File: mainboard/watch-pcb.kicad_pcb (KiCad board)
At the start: 6 copper layers, 42 x 42 mm, 179 parts, among them J10 LASER-, J11 MTR+, J13 MTR-, J2 USB_C_Receptacle, J3 ESP_ANT, J5 Micro_SD_Card, J6 TT143AMC12C, J7 BATT+, J8 BATT-, J9 LASER+, Q1 BSS214NW, Q2 BSS138, Q3 BSS138, SW1 B3U-3000P-B, SW2 B3U-3000P-B, SW3 B3U-3000P-B, SW4 B3U-3000P-B, SW8 BOOT, U1 TPS63021, U10 LIS3MDL, U11 ESP32-S3, U12 LSM6DSOXTR, U13 DRV2605LDGS, U14 MAX30102, U15 APDS-9306-065, U16 AP3019AK, U17 TLV62569DDC, U2 BQ25628E, U3 BME280, U4 BQ27427YZFR, U5 MX25UM51245GXDI00, U6 S80KS5123GABHV020, U8 TCA9535MRGER, U9 TPS65631W, Y1 32.768kHz, Y2 40MHz(10ppm)

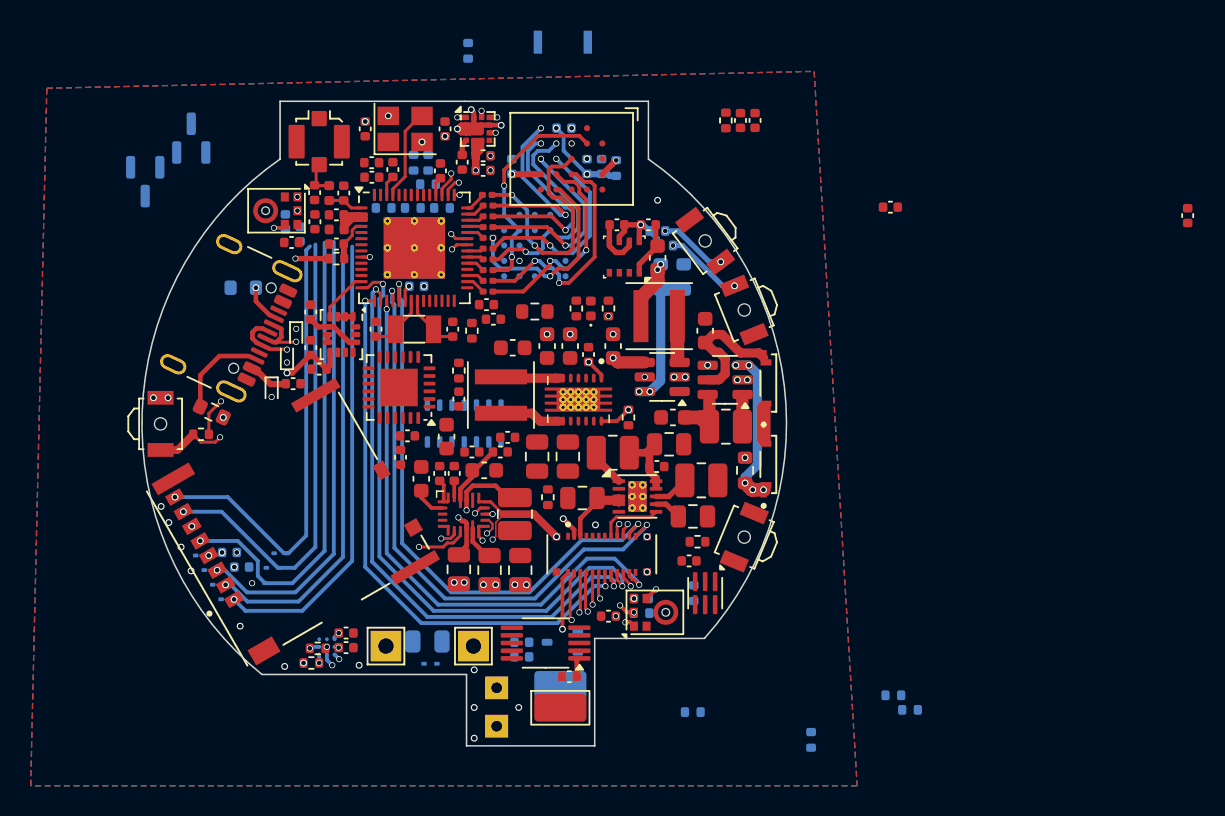
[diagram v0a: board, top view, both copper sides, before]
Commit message: mostly cleaned pcb after removals
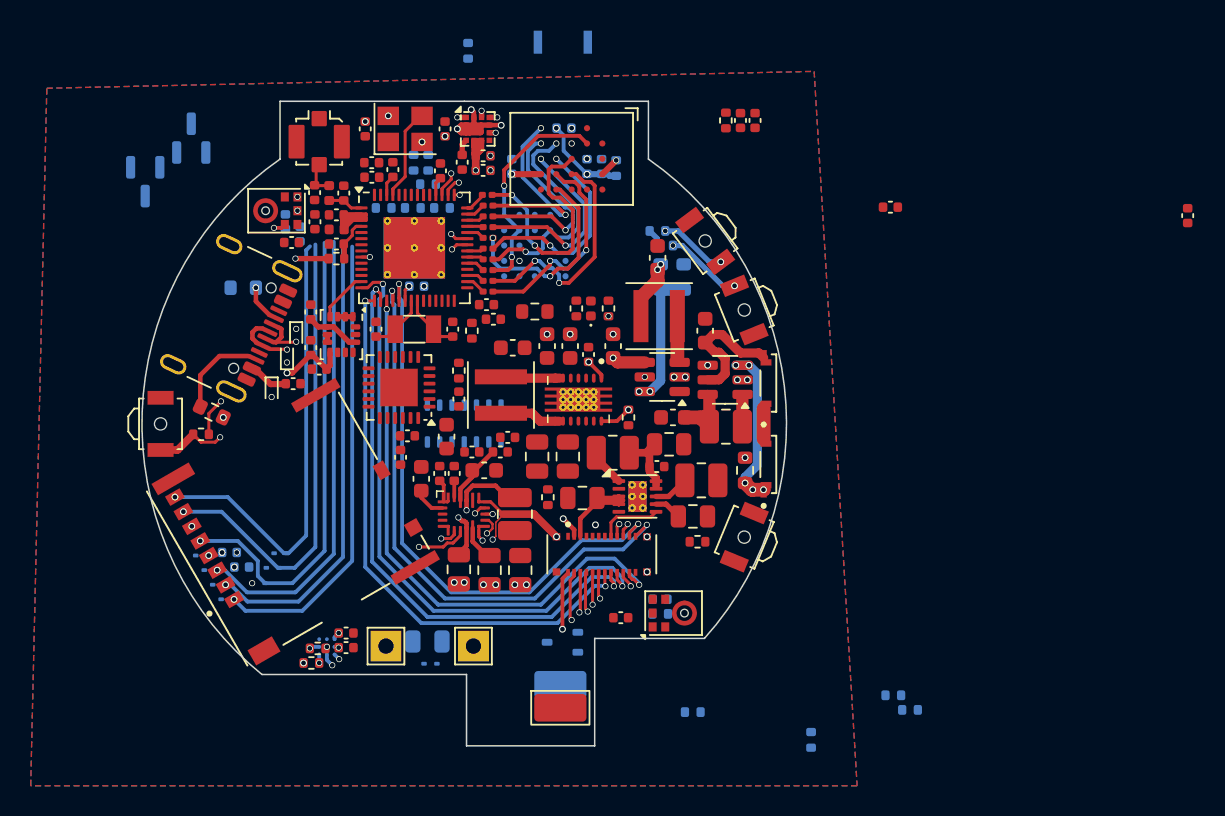
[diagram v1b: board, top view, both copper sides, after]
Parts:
- removed C52, C75, C78: 1uF, Capacitor_SMD:C_0402_1005Metric
- removed C54, C62, C71: 100nF, Capacitor_SMD:C_0402_1005Metric
- removed J11: MTR+, TestPoint:TestPoint_THTPad_1.5x1.5mm_Drill0.7mm
- removed J13: MTR-, TestPoint:TestPoint_THTPad_1.5x1.5mm_Drill0.7mm
- removed R5: 100k, Resistor_SMD:R_0402_1005Metric
- removed U13: DRV2605LDGS, Package_SO:VSSOP-10_3x3mm_P0.5mm
- removed U15: APDS-9306-065, OptoDevice:Broadcom_DFN-6_2x2mm_P0.65mm
- removed U3: BME280, Package_LGA:Bosch_LGA-8_2.5x2.5mm_P0.65mm_ClockwisePinNumbering
- moved R45 1.22 mm to (162.8, 95.9)
- moved C68 1.22 mm to (162.8, 95.0)
- moved MK2 1.22 mm to (163.6, 95.8)
- moved R36 0.81 mm to (160.2, 96.2)
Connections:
- J6 pad 15: /ESP MCU/EXT_IO3 -> /ESP MCU/EXT_IO2
- J6 pad 5: /ESP MCU/EXT_IO2 -> /ESP MCU/EXT_IO1
- R14 pad 1: /ESP MCU/EXT_IO10 -> /ESP MCU/EXT_IO9
- R15 pad 1: /ESP MCU/EXT_IO11 -> /ESP MCU/EXT_IO8
- R17 pad 1: /ESP MCU/EXT_IO12 -> /ESP MCU/EXT_IO7
- R47 pad 2: /ESP MCU/EXT_IO5 -> /ESP MCU/EXT_IO3
- R48 pad 2: /ESP MCU/EXT_IO6 -> /ESP MCU/EXT_IO4
- R49 pad 2: /ESP MCU/EXT_IO7 -> /ESP MCU/EXT_IO5
- SW2 pad 1: /ESP MCU/EXT_IO5 -> /ESP MCU/EXT_IO3
- SW3 pad 2: /ESP MCU/EXT_IO6 -> /ESP MCU/EXT_IO4
- SW4 pad 1: /ESP MCU/EXT_IO7 -> /ESP MCU/EXT_IO5
- U1 pad 13: /ESP MCU/EXT_IO10 -> /ESP MCU/EXT_IO9
- U10 pad 7: /ESP MCU/EXT_IO9 -> /ESP MCU/EXT_IO6
- U12 pad 9: /ESP MCU/EXT_IO4 -> /ESP MCU/IO7
- U2 pad 11: /ESP MCU/EXT_IO11 -> /ESP MCU/EXT_IO8
- U4 pad A1: /ESP MCU/EXT_IO12 -> /ESP MCU/EXT_IO7
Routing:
- net +3V3: track 48.0 -> 38.4 mm, vias 12 -> 10
- net GND: track 28.3 -> 21.4 mm, vias 54 -> 40
- net /ESP MCU/I2S_SCK: track 72.1 -> 65.4 mm, vias 3 -> 2
- net /ESP MCU/EXT_IO5: track 0.00 -> 5.10 mm, vias 0 -> 2
- net /ESP MCU/EXT_IO7: track 5.10 -> 0.55 mm, vias 2 -> 1
- net /ESP MCU/EXT_IO6: track 4.45 -> 0.00 mm, vias 2 -> 0
- net /ESP MCU/EXT_IO4: track 0.00 -> 4.45 mm, vias 0 -> 2
- net /ESP MCU/I2S_SD: track 63.2 -> 59.7 mm, vias 4 -> 2
- net /ESP MCU/I2S_WS: track 65.5 -> 62.6 mm, vias 3 -> 2
- net /ESP MCU/EXT_IO1: track 0.00 -> 2.10 mm, vias 0 -> 1
- net /ESP MCU/EXT_IO8: track 0.00 -> 1.55 mm, vias 0 -> 1
- net /ESP MCU/EXT_IO11: track 1.55 -> 0.00 mm, vias 1 -> 0
- net Net-(U13-REG): track 1.27 -> 0.00 mm
- net /ESP MCU/EXT_IO2: track 2.10 -> 0.91 mm
- net /ESP MCU/EXT_IO3: track 0.91 -> 0.00 mm, vias 1 -> 0
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
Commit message: more updates
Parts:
- removed C84: 10uF, Capacitor_SMD:C_0603_1608Metric
- R28, R29: moved to F.Cu
- moved D4 27.2 mm to (151.3, 102.3), turned to -90 degrees
- moved R13 26.8 mm to (152.3, 102.3), turned to 90 degrees
- moved R48 8.12 mm to (170.2, 68.1)
- moved R49 7.08 mm to (169.6, 69.2), turned to 180 degrees
- moved C81 6.33 mm to (162.4, 72.8), turned to 180 degrees
- moved R30 5.69 mm to (165.0, 75.0)
- moved U17 4.91 mm to (162.8, 75.5), turned to 90 degrees
- moved R29 4.18 mm to (160.2, 73.2)
- moved L3 3.40 mm to (162.7, 79.9)
- moved R28 3.29 mm to (160.3, 76.2), turned to 90 degrees
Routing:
- net +1V8: track 25.7 -> 13.9 mm, vias 6 -> 4
- net Net-(U17-FB): track 9.13 -> 0.00 mm, vias 2 -> 0
- net /ESP MCU/EXT_IO5: track 5.10 -> 0.00 mm, vias 2 -> 0
- net /USB and Power/1V8G: track 4.94 -> 0.00 mm, vias 2 -> 0
- net /ESP MCU/EXT_IO4: track 4.45 -> 0.00 mm, vias 2 -> 0
- net Net-(U17-SW): track 3.08 -> 0.00 mm
- net +VSW: track 9.95 -> 7.77 mm, vias 2 -> 1
- net +3V3: track 38.4 -> 37.3 mm
- net GND: track 21.4 -> 21.3 mm, vias 40 -> 37
